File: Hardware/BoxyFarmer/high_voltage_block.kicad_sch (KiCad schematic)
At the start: 27 parts

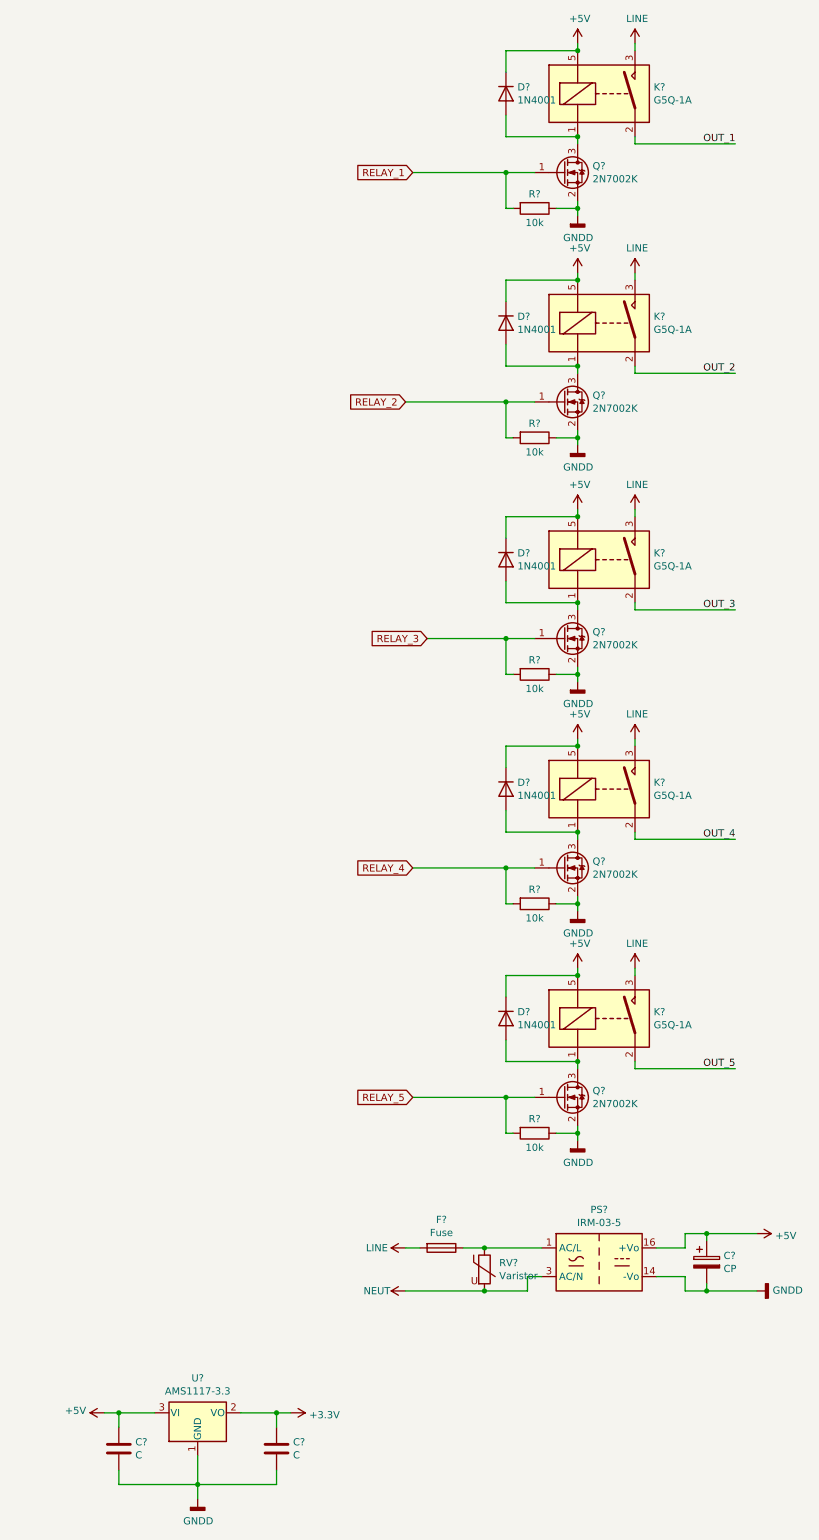
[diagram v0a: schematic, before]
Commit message: Changed Schematic structure, USB connector type changed from MicroUSB to MiniUSB
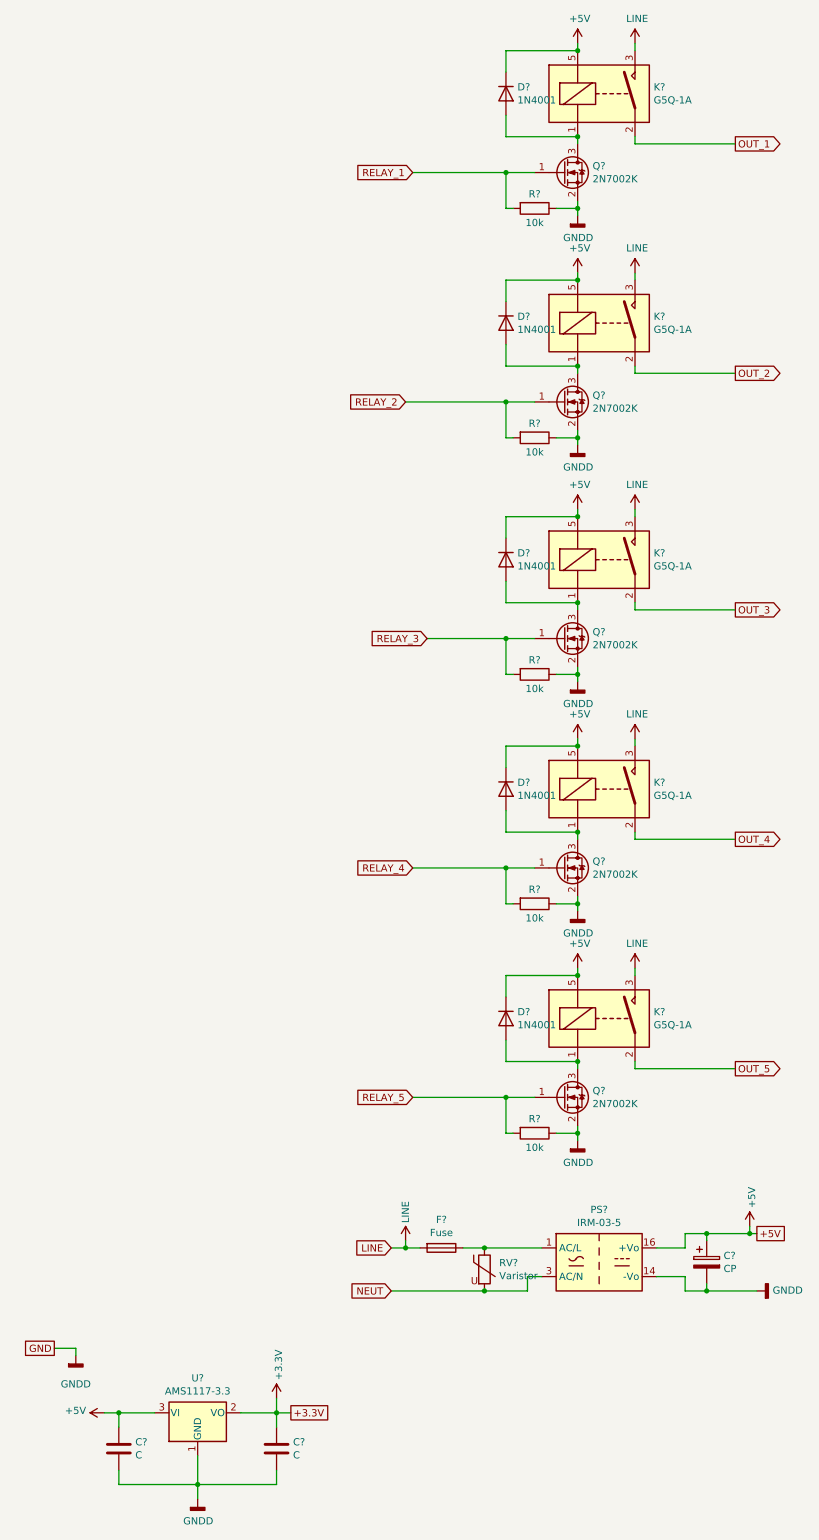
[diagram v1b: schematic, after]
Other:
- title: (none) -> BoxyFarmer
